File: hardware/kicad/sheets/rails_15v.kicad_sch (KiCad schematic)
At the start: 31 parts, among them U20 ADP5071AREZ, U21 ADP7142AUJZ, U22 ADP7182AUJZ

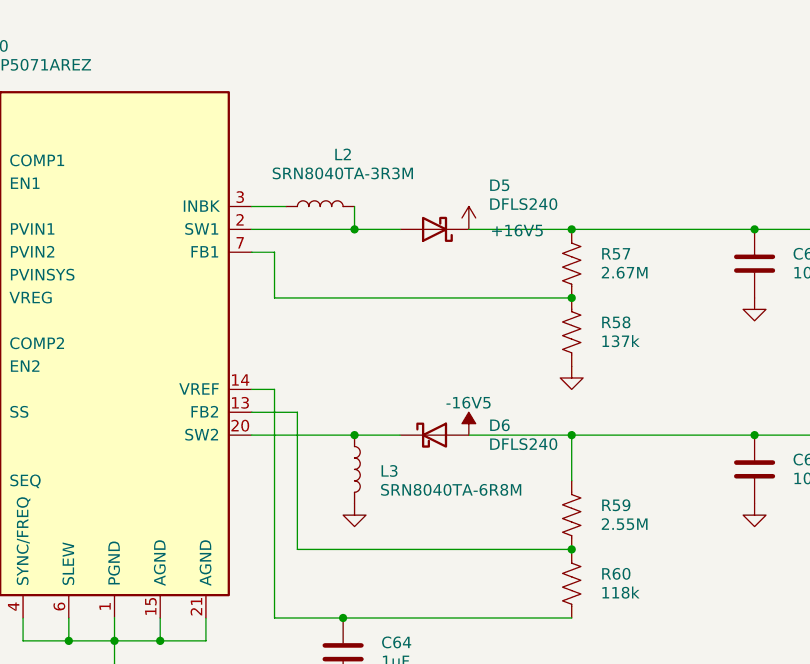
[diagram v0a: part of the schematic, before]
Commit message: Swap L2/L3 for shielded Bourns SRP7050TA inductors
L2 (3.3 uH boost) and L3 (6.8 uH inverting) were semi-shielded SRN8040TA
parts. Replace them with fully shielded SRP7050TA-3R3M / -6R8M, using a
new L_Bourns_SRP7050TA footprint (datasheet land pattern, 7.3 x 6.6 mm
body) and a 5.0 mm envelope model. The routed board keeps its tracks (the
footprints were swapped in place and the pours refilled); DRC 0 errors,
0 unconnected. Gerbers and BOM regenerated.

Co-Authored-By: Claude Sonnet 5.5 <noreply@anthropic.com>
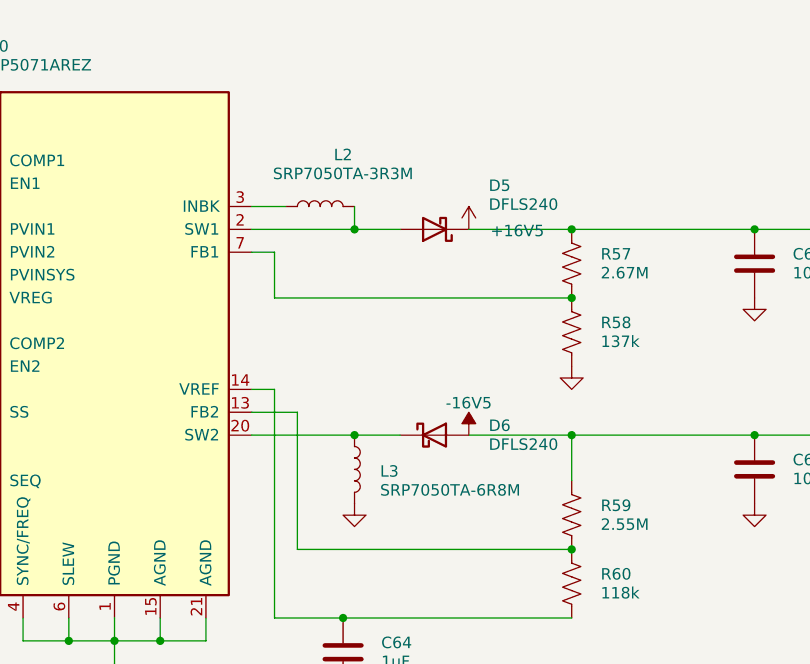
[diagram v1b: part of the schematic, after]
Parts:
- L2: value SRN8040TA-3R3M -> SRP7050TA-3R3M; footprint Inductor_SMD:L_Bourns_SRN8040TA -> cryocooler:L_Bourns_SRP7050TA
- L3: value SRN8040TA-6R8M -> SRP7050TA-6R8M; footprint Inductor_SMD:L_Bourns_SRN8040TA -> cryocooler:L_Bourns_SRP7050TA
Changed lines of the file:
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@@
 			)
 		)
-		(property "Value" "SRN8040TA-3R3M"
+		(property "Value" "SRP7050TA-3R3M"
 			(at 165.1 108.1277 270)
 			(show_name no)
@@
 			)
 		)
-		(property "Footprint" "Inductor_SMD:L_Bourns_SRN8040TA"
+		(property "Footprint" "cryocooler:L_Bourns_SRP7050TA"
 			(at 162.56 111.76 0)
 			(hide yes)
@@
 			)
 		)
-		(property "Value" "SRN8040TA-6R8M"
+		(property "Value" "SRP7050TA-6R8M"
 			(at 169.2023 143.29 0)
 			(show_name no)
@@
 			)
 		)
-		(property "Footprint" "Inductor_SMD:L_Bourns_SRN8040TA"
+		(property "Footprint" "cryocooler:L_Bourns_SRP7050TA"
 			(at 166.37 140.97 0)
 			(hide yes)

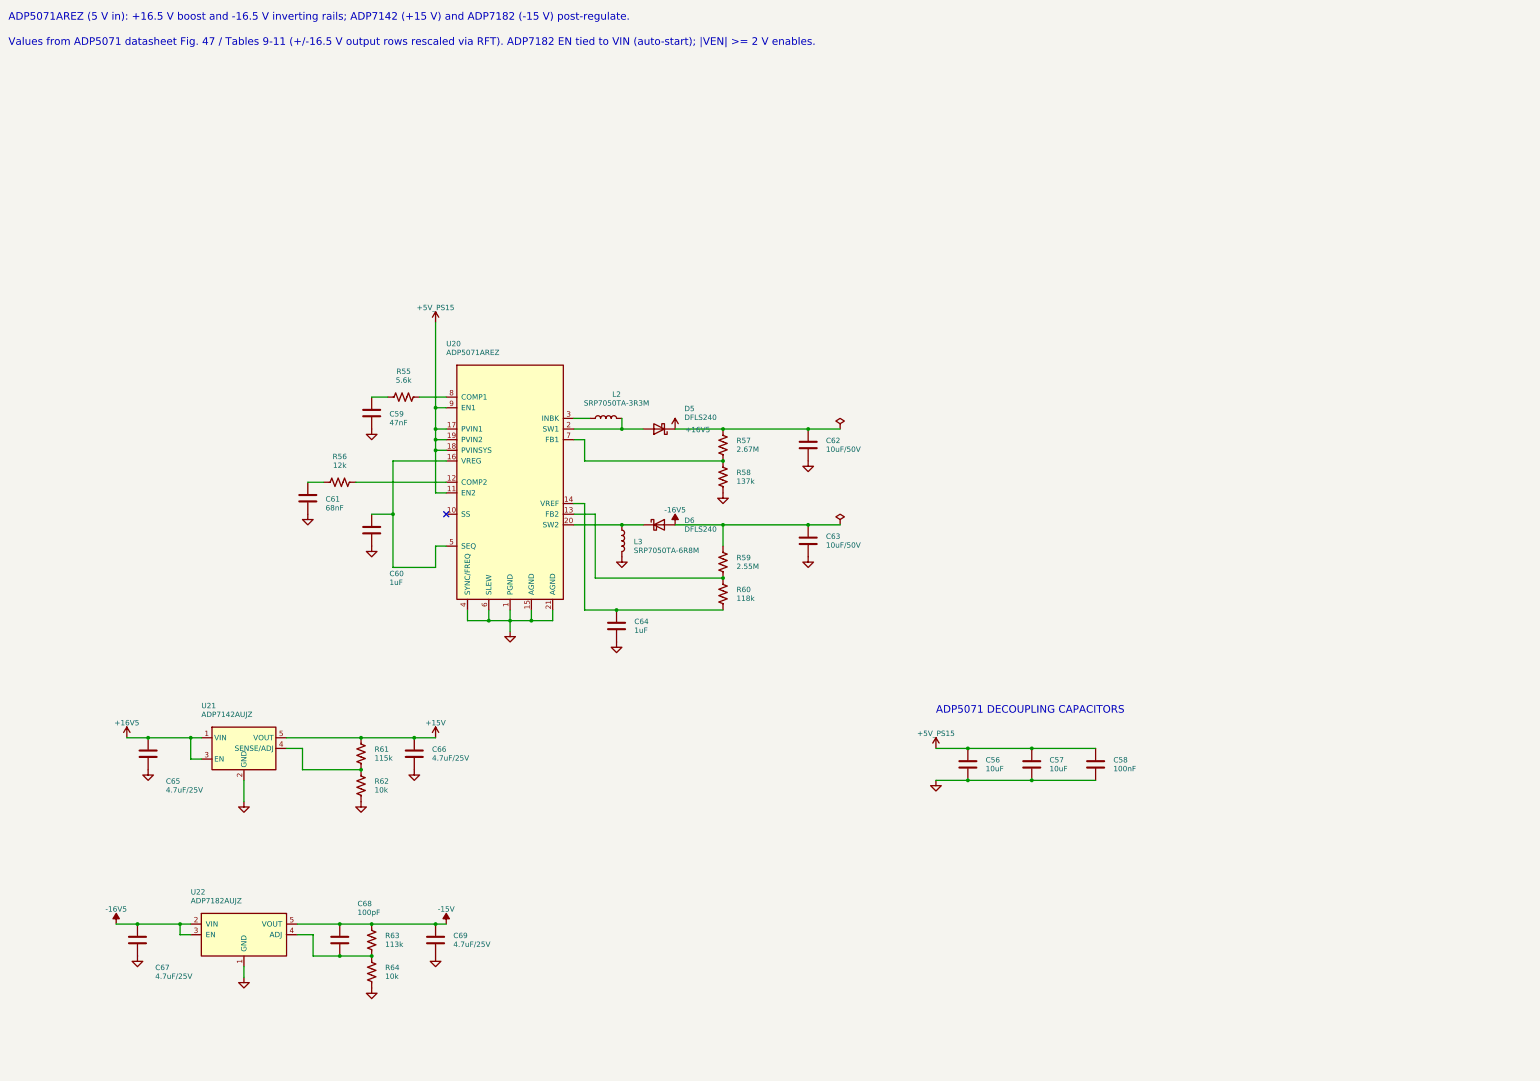
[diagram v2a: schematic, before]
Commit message: Replace the ±15 V LDOs with one LT3097 and add a power-good interlock
- rails_15v: ADP7142 + ADP7182 replaced by one LT3097 (±14.7 V, 147 k SET
  resistors); the ADP5071 output caps are now 22 uF / 50 V and double as the
  LT3097 inputs. PGP / PGN make the PG_15V node (fed from +15 V, so it reads
  0 V if a rail is missing).
- amp_control: a series BSS138 (Q9) gated by PG_15V blocks AMP_REM unless
  both rails are good. New power_good sheet: LED (D23) and the active-low
  PG_15V_N flag on GPIO43 (PG_15V_N_PIN).
- Tooling: LT3097 symbol, footprint and 3D envelope; datasheet rules (191),
  GPIO check, BOM tables, floor plan, PAD_BRIDGES and pre-placed GND vias in
  gen_pcb.py, new fix_route.py for post-route clean-up.
- Board regenerated and routed with Freerouting 2.5.0: DRC 0 unconnected,
  0 schematic-parity issues, no copper violations. Gerbers, JLCPCB zip,
  renders, BOM, CPL and schematic PDF regenerated.

Co-Authored-By: Claude Sonnet 5.5 <noreply@anthropic.com>
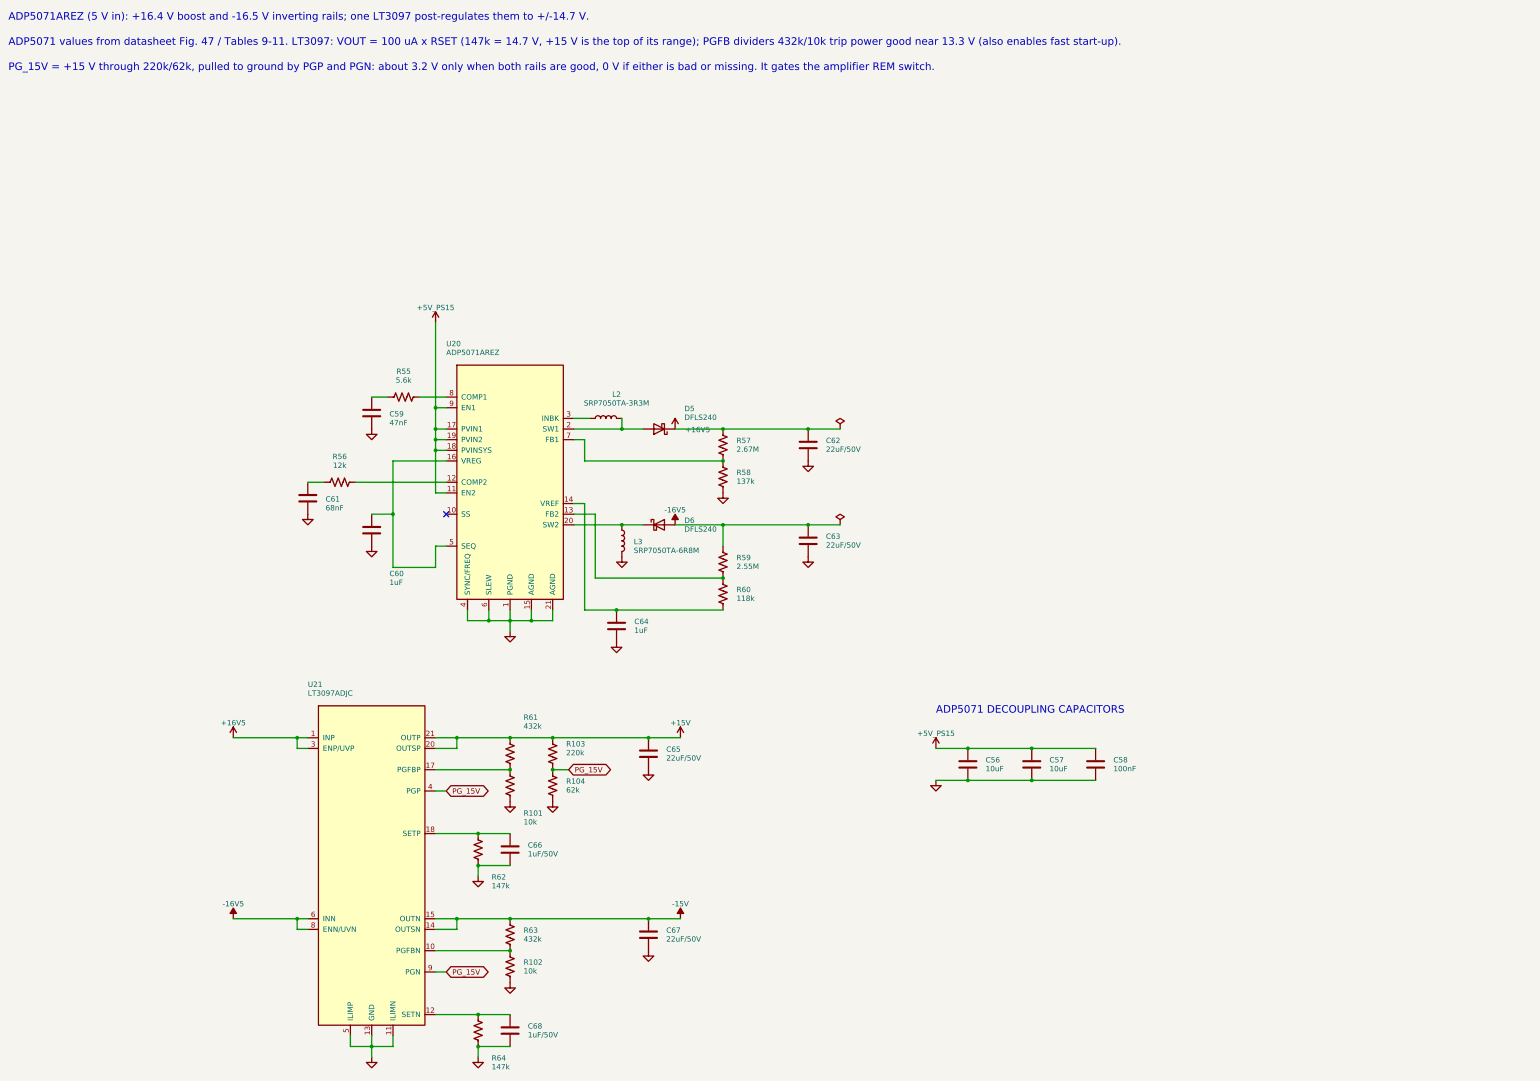
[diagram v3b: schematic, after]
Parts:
- removed C56: 10uF, Capacitor_SMD:C_0805_2012Metric, symbol Device:C
- removed C65: 4.7uF/25V, Capacitor_SMD:C_1206_3216Metric, symbol Device:C
- removed L2: SRP7050TA-3R3M, cryocooler:L_Bourns_SRP7050TA, symbol Device:L
- removed R56: 12k, Resistor_SMD:R_0603_1608Metric, symbol Device:R_US
- removed R57: 2.67M, Resistor_SMD:R_0603_1608Metric, symbol Device:R_US
- removed R59: 2.55M, Resistor_SMD:R_0603_1608Metric, symbol Device:R_US
- removed R62: 10k, Resistor_SMD:R_0603_1608Metric, symbol Device:R_US
- removed U21: ADP7142AUJZ, Package_TO_SOT_SMD:TSOT-23-5, symbol Regulator_Linear:ADP7142AUJZ
- added C59: 47nF, Capacitor_SMD:C_1206_3216Metric, symbol Device:C
- added C61: 68nF, Capacitor_SMD:C_1206_3216Metric, symbol Device:C
- added C63: 22uF/50V, Capacitor_SMD:C_1210_3225Metric, symbol Device:C
- added C66: 1uF/50V, Capacitor_SMD:C_1206_3216Metric, symbol Device:C
- added D5: DFLS240, Diode_SMD:D_PowerDI-123, symbol Device:D_Schottky
- added R103: 220k, Resistor_SMD:R_0603_1608Metric, symbol Device:R_US
- added R104: 62k, Resistor_SMD:R_0603_1608Metric, symbol Device:R_US
- added R58: 137k, Resistor_SMD:R_0603_1608Metric, symbol Device:R_US
- added R61: 432k, Resistor_SMD:R_0603_1608Metric, symbol Device:R_US
- added U21: LT3097ADJC, cryocooler:DFN-22-2EP_6x3mm_P0.5mm_LT3097, symbol cryocooler:LT3097ADJC
- C57: renamed from C58; value 100nF -> 10uF; footprint Capacitor_SMD:C_0603_1608Metric -> Capacitor_SMD:C_0805_2012Metric
- C58: renamed from R55; value 5.6k -> 100nF; footprint Resistor_SMD:R_0603_1608Metric -> Capacitor_SMD:C_0603_1608Metric; symbol Device:R_US -> Device:C
- C62: value 10uF/50V -> 22uF/50V
- C65: renamed from R61; value 115k -> 22uF/50V; footprint Resistor_SMD:R_0603_1608Metric -> Capacitor_SMD:C_1210_3225Metric; symbol Device:R_US -> Device:C
- C67: value 4.7uF/25V -> 22uF/50V; footprint Capacitor_SMD:C_1206_3216Metric -> Capacitor_SMD:C_1210_3225Metric
- C68: renamed from C69; value 4.7uF/25V -> 1uF/50V
- L2: renamed from D5; value DFLS240 -> SRP7050TA-3R3M; footprint Diode_SMD:D_PowerDI-123 -> cryocooler:L_Bourns_SRP7050TA; symbol Device:D_Schottky -> Device:L
- R101: renamed from C66; value 4.7uF/25V -> 10k; footprint Capacitor_SMD:C_1206_3216Metric -> Resistor_SMD:R_0603_1608Metric; symbol Device:C -> Device:R_US
- R55: renamed from C59; value 47nF -> 5.6k; footprint Capacitor_SMD:C_1206_3216Metric -> Resistor_SMD:R_0603_1608Metric; symbol Device:C -> Device:R_US
- R56: renamed from C61; value 68nF -> 12k; footprint Capacitor_SMD:C_1206_3216Metric -> Resistor_SMD:R_0603_1608Metric; symbol Device:C -> Device:R_US
- R57: renamed from R58; value 137k -> 2.67M
- R59: renamed from R60; value 118k -> 2.55M
- R60: renamed from C63; value 10uF/50V -> 118k; footprint Capacitor_SMD:C_1210_3225Metric -> Resistor_SMD:R_0603_1608Metric; symbol Device:C -> Device:R_US
- R62: renamed from U22; value ADP7182AUJZ -> 147k; footprint Package_TO_SOT_SMD:TSOT-23-5 -> Resistor_SMD:R_0603_1608Metric; symbol cryocooler:ADP7182AUJZ -> Device:R_US
- R63: value 113k -> 432k
- R64: renamed from C68; value 100pF -> 147k; footprint Capacitor_SMD:C_1206_3216Metric -> Resistor_SMD:R_0603_1608Metric; symbol Device:C -> Device:R_US
- renumbered C57 to C56, R64 to R102
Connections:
- net +15V: now also R103.1, R61.1, U21.20 (OUTSP), U21.21 (OUTP), U21.22 (OUTP); no longer R101.1
- net +16V5: now also R57.1, D5.1 (K), U21.1 (INP), U21.2 (INP), U21.3 (ENP/UVP); no longer L2.1 (K)
- net +5V_PS15: now also C58.1
- net -15V: now also C67.1, U21.14 (OUTSN), U21.15 (OUTN), U21.16 (OUTN); no longer C68.1, R62.5 (VOUT), R64.1
- net -16V5: now also R59.1, C63.1, U21.24 (INN), U21.6 (INN), U21.7 (INN), U21.8 (ENN/UVN); no longer C67.1, R60.1, R62.2 (VIN), R62.3 (EN)
- net GND: now also C58.2, C65.2, R62.2, R64.2, C59.2, C61.2, C63.2, C66.2, R104.2, R58.2, U21.11 (ILIMN), U21.13 (GND), U21.19 (GND), U21.23 (GND), U21.5 (ILIMP); no longer R55.2, R56.2, R57.2, R60.2, R62.1 (GND)
- net at R102.1, R63.2: now also U21.10 (PGFBN); no longer R62.4 (ADJ), R64.2
- net at U20.7 (FB1): now also R57.2, R58.1; no longer R57.1
- net at U20.13 (FB2): now also R59.2, R60.1; no longer R59.1
- net at C64.1, U20.14 (VREF): now also R60.2; no longer R59.2
- net at R55.1: now also C59.1; no longer C58.1
- net at U20.8 (COMP1): now also R55.2; no longer C58.2
- net at R56.1: now also C61.1
- net at U20.3 (INBK): now also L2.1
- net at L2.2, U20.2 (SW1): now also D5.2 (A)
- net at U20.12 (COMP2): now also R56.2
- new net: C68.1, R64.1, U21.12 (SETN)
- new net: R101.1, R61.2, U21.17 (PGFBP)
- new net: C66.1, R62.1, U21.18 (SETP)
- new net PG_15V: R103.2, R104.1, U21.4 (PGP), U21.9 (PGN)
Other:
- note added: "ADP5071 values from datasheet Fig. 47 / Tables 9-11. LT3097: VOUT = 100 uA x RSET (147k = 14.7 V, +15 V is the top of its range); PGFB dividers 432k/10k trip power good near 13.3 V (also enables fast start-up)."
- note added: "ADP5071AREZ (5 V in): +16.4 V boost and -16.5 V inverting rails; one LT3097 post-regulates them to +/-14.7 V."
- note added: "PG_15V = +15 V through 220k/62k, pulled to ground by PGP and PGN: about 3.2 V only when both rails are good, 0 V if either is bad or missing. It gates the amplifier REM switch."
- note removed: "ADP5071AREZ (5 V in): +16.5 V boost and -16.5 V inverting rails; ADP7142 (+15 V) and ADP7182 (-15 V) post-regulate."
- note removed: "Values from ADP5071 datasheet Fig. 47 / Tables 9-11 (+/-16.5 V output rows rescaled via RFT). ADP7182 EN tied to VIN (auto-start); |VEN| >= 2 V enables."
- moved on the sheet: C56, C57, C68, R102, R57, R59, R63

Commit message: Log +-15 V power-good changes and add one LED per LT3097 PG pin
Firmware
- amplifier: configure PG_15V_N_PIN (GPIO43, active LOW), log the starting
  state and every debounced change (PowerGoodMonitor in power_good.h);
  amplifier::isPowerGood() reports the level. The lines reach the dashboard
  console through the logger ring buffer.
- dashboard: console colours for "power lost" (red), "power restored" and
  "power good: yes" (green), "power good: no" (yellow).
- native tests for the debounce logic and the amplifier stub.

Hardware
- power_good sheet: PGP and PGN each drive their own node (220k/62k from
  +15 V) and a green LED (D24 +15 V, D25 -15 V) through a BSS138W; a BAT54AW
  with a 10k pull-up ANDs the nodes into PG_15V, so the REM interlock and the
  PG_15V_N flag are unchanged.
- 0402 resistors, SOT-323 FETs and one BAT54AW so the stage fits the power
  box; Power Good parts are placed last in gen_pcb.py.
- Board re-routed with Freerouting 2.5.0 and cleaned with fix_route.py: DRC
  0 unconnected, no copper violations. Gerbers, JLCPCB zip, renders, BOM, CPL
  and schematic PDF regenerated; datasheet rules 193/193.

Co-Authored-By: Claude Sonnet 5.5 <noreply@anthropic.com>
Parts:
- removed R103: 220k, Resistor_SMD:R_0603_1608Metric, symbol Device:R_US
- removed R104: 62k, Resistor_SMD:R_0603_1608Metric, symbol Device:R_US
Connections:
- net PG_15V renamed PGN_15V
- net PGN_15V: no longer U21.4 (PGP)
- new net PGP_15V: U21.4 (PGP)
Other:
- note added: "PGP and PGN (open collector, low = bad) go to nodes PGP_15V / PGN_15V built on the power_good sheet, which also makes PG_15V and lights one LED per pin."
- note removed: "PG_15V = +15 V through 220k/62k, pulled to ground by PGP and PGN: about 3.2 V only when both rails are good, 0 V if either is bad or missing. It gates the amplifier REM switch."
